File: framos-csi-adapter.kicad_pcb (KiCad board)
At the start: 4 copper layers, 26.5 x 26.5 mm, 69 parts, among them J1 Socket_Hirose_DF40_2x30_DF40C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, J2 Conn_STM_MSAK24025P30, U1 NTS0102_XSON, U2 AP62301Z6-7, U3 AP62301Z6-7

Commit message: [#56796] Update revision & date
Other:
- board text added: "FRAMOS CSI adapter Rev. 1.1.2 03/2024"
- board text removed: "FRAMOS CSI adapter Rev. 1.1.1 10/2023"

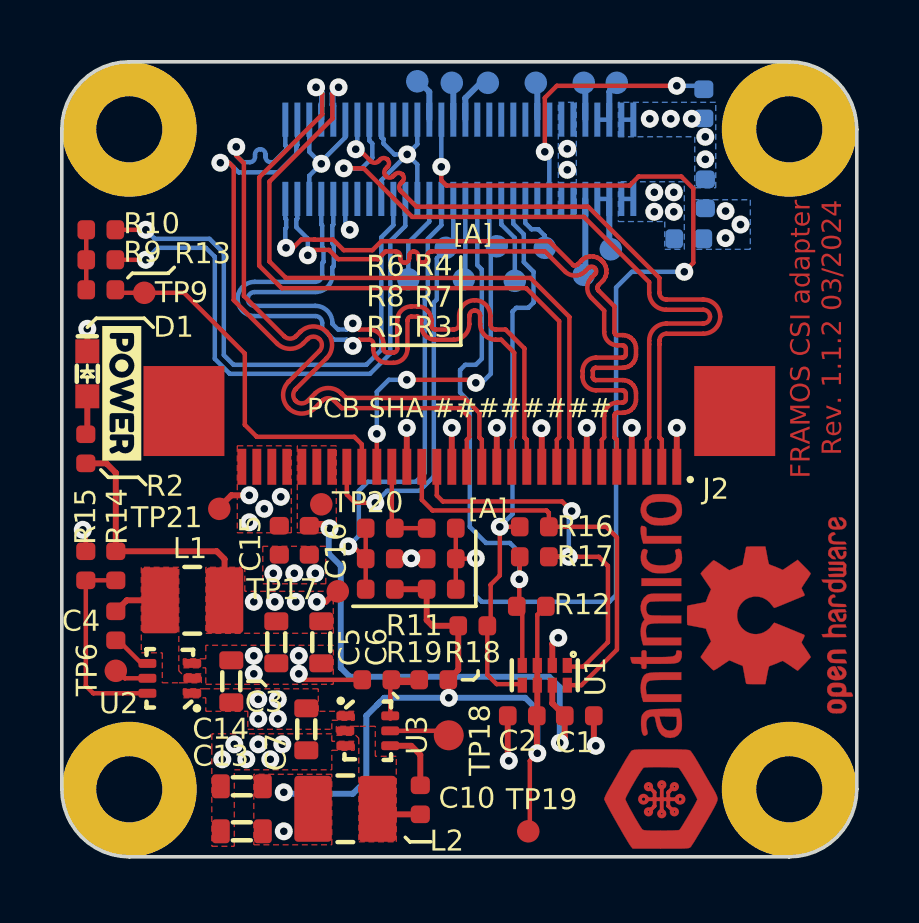
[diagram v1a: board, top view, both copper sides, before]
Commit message: [#56796] Small PCB fixes, DNP marking
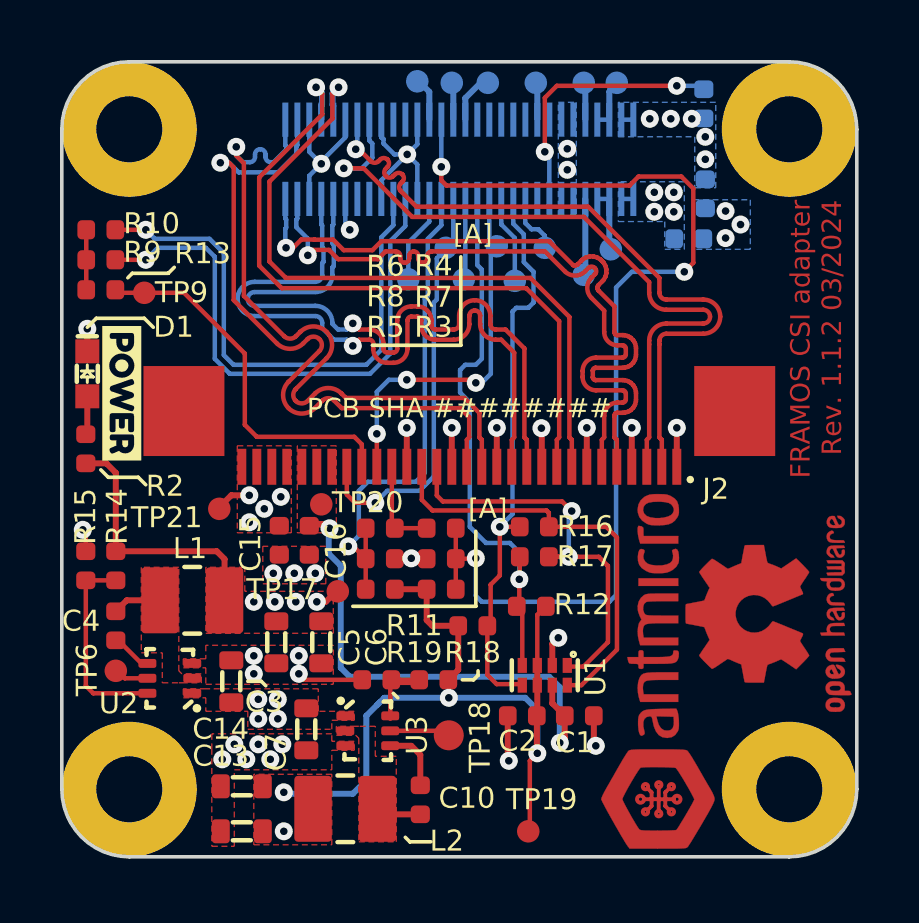
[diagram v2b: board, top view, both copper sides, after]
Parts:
- removed N1: oshw_logo, framos-csi-adapter-footprints:OSHW-Logo2_7.3x6mm_Copper_Mask
- removed N2: antmicro_logo, framos-csi-adapter-footprints:antmicro-logo_scaled_12mm
- added REF**: OSHW-Logo2_7.3x6mm_Copper_Mask, antmicro-footprints:OSHW-Logo2_7.3x6mm_Copper_Mask, F.Cu at (123.5, 118.4)
- added REF**: LOGO, antmicro-footprints:antmicro-logo_scaled_12mm, F.Cu at (119.9, 120.3)
- TP18: footprint framos-csi-adapter-footprints:Testpoint_smd_1mm -> antmicro-footprints:TP_SMD_1mm
